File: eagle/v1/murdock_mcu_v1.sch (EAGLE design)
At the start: 30 parts, among them IC1 MPU-9150, IC2 LT1763CS8-3.3, IC3 STM32F4XX_64, U1 USD-SOCKETNEW, X1 USBSMD, X2 MURDOCK_STACK

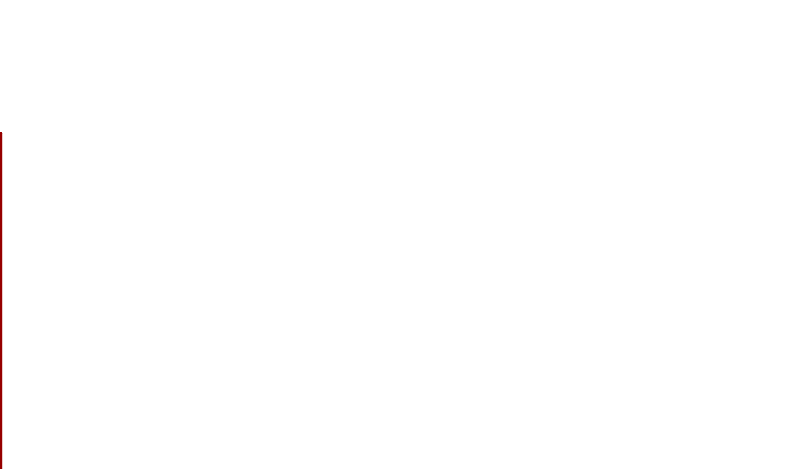
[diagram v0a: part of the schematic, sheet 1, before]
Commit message: updated labels
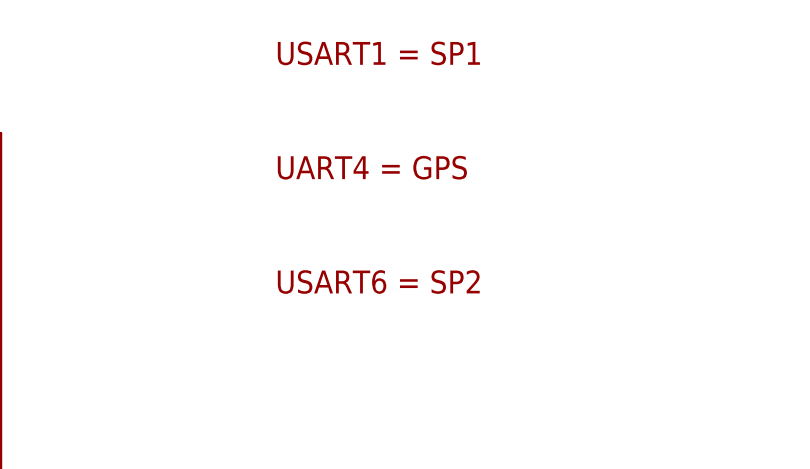
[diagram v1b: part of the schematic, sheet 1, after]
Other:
- note added: "UART4 = GPS"
- note added: "USART1 = SP1"
- note added: "USART6 = SP2"
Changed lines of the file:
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@@
 <plain>
 <text x="-93.98" y="60.96" size="1.778" layer="91">defined value on the bootloader pins</text>
+<text x="99.06" y="170.18" size="2.54" layer="94">UART4 = GPS</text>
+<text x="99.06" y="182.88" size="2.54" layer="94">USART1 = SP1</text>
+<text x="99.06" y="157.48" size="2.54" layer="94">USART6 = SP2</text>
 </plain>
 <instances>
